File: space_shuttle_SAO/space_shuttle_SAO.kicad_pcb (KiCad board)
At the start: 2 copper layers, 80 x 49.8 mm, 4 parts, among them J1 SAO_1.69

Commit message: Working on the main village base badge
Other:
- net class Default removed

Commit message: updated per latest protoype discoveries
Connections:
- J1 pad 3: Net-(J1-Pad3) -> unconnected-(J1-Pad3)
- J1 pad 4: Net-(J1-Pad4) -> unconnected-(J1-Pad4)
- J1 pad 5: Net-(J1-Pad5) -> unconnected-(J1-Pad5)
- J1 pad 6: Net-(J1-Pad6) -> unconnected-(J1-Pad6)
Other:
- board text added: "aerospacevillage.org"
- board text added: "v03"
- board text removed: "v0.2"
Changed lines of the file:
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@@
   )
   (paper "A4")
+  (title_block
+    (title "Space Shuttle SAO")
+    (date "2022-05-22")
+    (rev "v03")
+    (company "Aerospace Village")
+    (comment 1 "Author: Dan Allen")
+  )
   (layers
     (0 "F.Cu" signal)
@@
   (net 2 "GND")
   (net 3 "Net-(J1-Pad1)")
-  (net 4 "Net-(J1-Pad3)")
-  (net 5 "Net-(J1-Pad4)")
-  (net 6 "Net-(J1-Pad5)")
-  (net 7 "Net-(J1-Pad6)")
+  (net 4 "unconnected-(J1-Pad3)")
+  (net 5 "unconnected-(J1-Pad4)")
+  (net 6 "unconnected-(J1-Pad5)")
+  (net 7 "unconnected-(J1-Pad6)")
   (footprint "space_shuttle_SAO:space_shuttle_proper" (layer "F.Cu")
     (at 140.51788 73.48728)
@@
   (footprint "space_shuttle_SAO:sao_1.69" (layer "F.Cu")
     (at 115.019626 99.883299 -20)
+    (property "Sheetfile" "space_shuttle_SAO.kicad_sch")
+    (property "Sheetname" "")
     (attr through_hole)
     (fp_text reference "J1" (at -0.04318 2.9337 160) (layer "F.SilkS") hide
@@
     )
     (pad "1" thru_hole rect locked (at -2.54 -1.27 340) (size 1.524 1.524) (drill 0.762) (layers *.Cu *.Mask)
-      (net 3 "Net-(J1-Pad1)"))
+      (net 3 "Net-(J1-Pad1)") (pinfunction "VCC") (pintype "passive"))
     (pad "2" thru_hole circle locked (at -2.54 1.27 340) (size 1.524 1.524) (drill 0.762) (layers *.Cu *.Mask)
-      (net 2 "GND"))
+      (net 2 "GND") (pinfunction "GND") (pintype "passive"))
     (pad "3" thru_hole circle locked (at 0 -1.27 340) (size 1.524 1.524) (drill 0.762) (layers *.Cu *.Mask)
-      (net 4 "Net-(J1-Pad3)"))
+      (net 4 "unconnected-(J1-Pad3)") (pinfunction "SDA") (pintype "passive+no_connect"))
     (pad "4" thru_hole circle locked (at 0 1.27 340) (size 1.524 1.524) (drill 0.762) (layers *.Cu *.Mask)
-      (net 5 "Net-(J1-Pad4)"))
+      (net 5 "unconnected-(J1-Pad4)") (pinfunction "SCL") (pintype "passive+no_connect"))
     (pad "5" thru_hole circle locked (at 2.54 -1.27 340) (size 1.524 1.524) (drill 0.762) (layers *.Cu *.Mask)
-      (net 6 "Net-(J1-Pad5)"))
+      (net 6 "unconnected-(J1-Pad5)") (pinfunction "GPIO_1") (pintype "passive+no_connect"))
     (pad "6" thru_hole circle locked (at 2.54 1.27 340) (size 1.524 1.524) (drill 0.762) (layers *.Cu *.Mask)
-      (net 7 "Net-(J1-Pad6)"))
+      (net 7 "unconnected-(J1-Pad6)") (pinfunction "GPIO_2") (pintype "passive+no_connect"))
   )
   (footprint "sunled:XZMYK45WT-9" (layer "B.Cu")
     (at 166.670202 106.777002 -45)
+    (property "Sheetfile" "space_shuttle_SAO.kicad_sch")
+    (property "Sheetname" "")
     (attr through_hole)
     (fp_text reference "D1" (at 5.10286 0.325119 45) (layer "B.SilkS")
@@
       (effects (font (size 1 1) (thickness 0.15)))
     )
-    (fp_circle (center 3.673303 1.655371) (end 3.873303 1.655371) (layer "B.SilkS") (width 0.4) (fill none))
+    (fp_circle (center -3.69824 -1.5621) (end -3.49824 -1.5621) (layer "B.SilkS") (width 0.4) (fill none))
     (fp_circle (center -0.01524 -0.14214) (end 0.78476 -0.14214) (layer "B.Mask") (width 1.6) (fill none))
     (pad "1" smd rect locked (at -2.6 0 315) (size 1.4 2.6) (layers "B.Cu" "B.Paste" "B.Mask")
-      (net 2 "GND"))
+      (net 2 "GND") (pinfunction "K") (pintype "passive"))
     (pad "2" smd rect locked (at 2.6 0 315) (size 1.4 2.6) (layers "B.Cu" "B.Paste" "B.Mask")
-      (net 1 "Net-(D1-Pad2)"))
+      (net 1 "Net-(D1-Pad2)") (pinfunction "A") (pintype "passive"))
   )
   (footprint "Resistors_SMD:R_1206_3216Metric" (layer "B.Cu")
@@
     (descr "Resistor SMD 1206 (3216 Metric), square (rectangular) end terminal, IPC_7351 nominal, (Body size source: IPC-SM-782 page 72, https://www.pcb-3d.com/wordpress/wp-content/uploads/ipc-sm-782a_amendment_1_and_2.pdf), generated with kicad-footprint-generator")
     (tags "resistor")
+    (property "Sheetfile" "space_shuttle_SAO.kicad_sch")
+    (property "Sheetname" "")
     (attr smd)
     (fp_text reference "R1" (at 0 1.82 -45) (layer "B.SilkS")
@@
     (fp_line (start 1.6 -0.8) (end -1.6 -0.8) (layer "B.Fab") (width 0.1))
     (pad "1" smd roundrect locked (at -1.4625 0 315) (size 1.125 1.75) (layers "B.Cu" "B.Paste" "B.Mask") (roundrect_rratio 0.2222204444)
-      (net 3 "Net-(J1-Pad1)"))
+      (net 3 "Net-(J1-Pad1)") (pintype "passive"))
     (pad "2" smd roundrect locked (at 1.4625 0 315) (size 1.125 1.75) (layers "B.Cu" "B.Paste" "B.Mask") (roundrect_rratio 0.2222204444)
-      (net 1 "Net-(D1-Pad2)"))
+      (net 1 "Net-(D1-Pad2)") (pintype "passive"))
     (model "${KISYS3DMOD}/Resistor_SMD.3dshapes/R_1206_3216Metric.wrl"
       (offset (xyz 0 0 0))
@@
     )
   )
-  (gr_text "v0.2" (at 108.51896 115.7224) (layer "B.Cu")
+  (gr_text "v03" (at 108.51896 115.7224) (layer "B.Cu")
     (effects (font (size 1.5 1.5) (thickness 0.3)) (justify mirror))
   )
@@
     (effects (font (size 1 1) (thickness 0.15)) (justify mirror))
   )
-  (gr_text "SAO V.1.69" (at 117.094 95.81896) (layer "B.SilkS")
+  (gr_text "aerospacevillage.org" (at 136.121177 96.432338 -20) (layer "B.SilkS")
+    (effects (font (size 3 3) (thickness 0.5)) (justify mirror))
+  )
+  (gr_text "SAO V.1.69" (at 116.934329 95.213789 -20) (layer "B.SilkS")
     (effects (font (size 1 1) (thickness 0.15)) (justify mirror))
   )
@@
   (zone (net 2) (net_name "GND") (layer "F.Cu") (hatch edge 0.508)
     (connect_pads (clearance 0.508))
-    (min_thickness 0.254)
+    (min_thickness 0.254) (filled_areas_thickness no)
     (fill yes (thermal_gap 0.508) (thermal_bridge_width 0.508))
     (polygon
@@
   (zone (net 2) (net_name "GND") (layer "B.Cu") (hatch edge 0.508)
     (connect_pads (clearance 0.508))
-    (min_thickness 0.254)
+    (min_thickness 0.254) (filled_areas_thickness no)
     (fill yes (thermal_gap 0.508) (thermal_bridge_width 0.508))
     (polygon

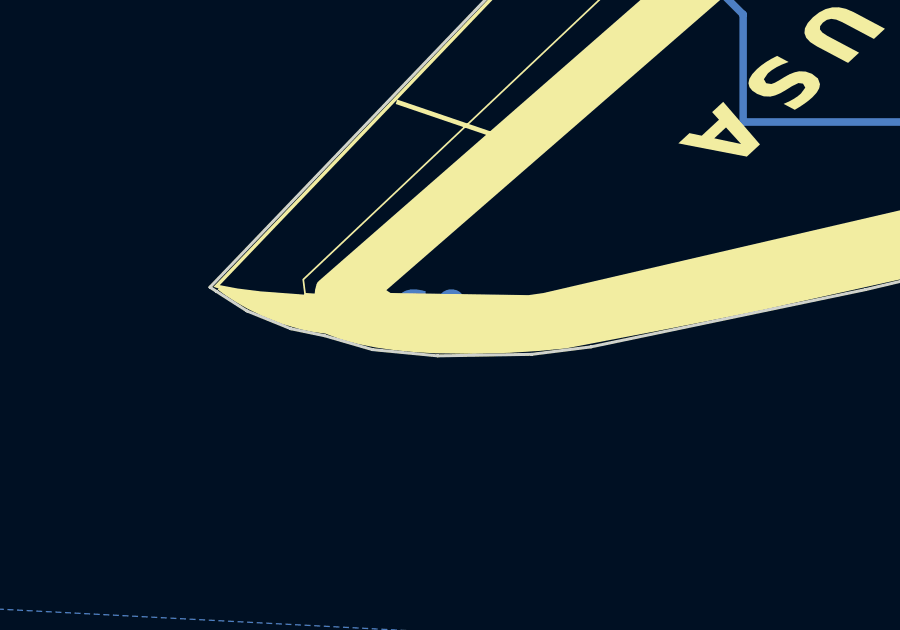
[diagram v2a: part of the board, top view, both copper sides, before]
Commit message: updated base badge, shuttle, and warning
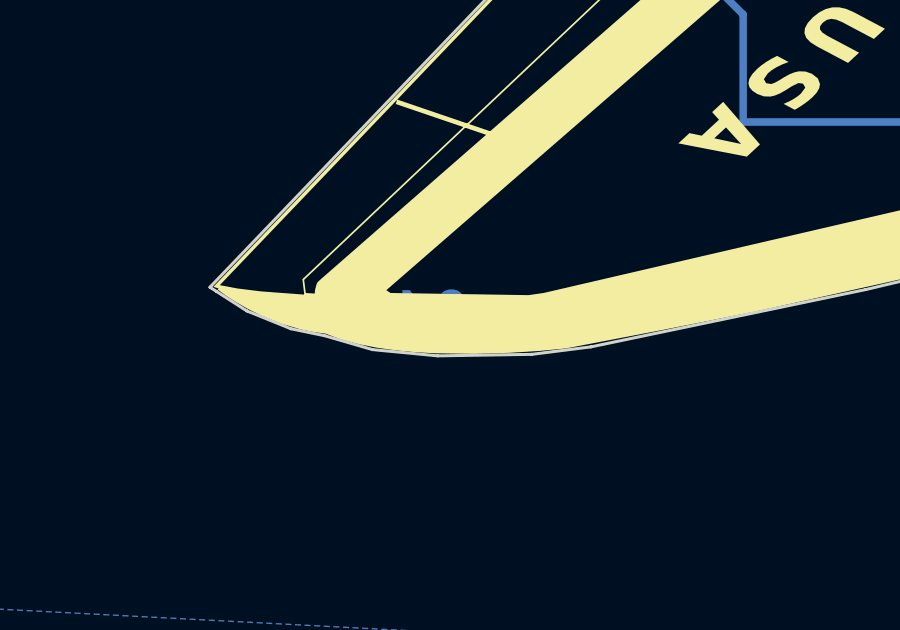
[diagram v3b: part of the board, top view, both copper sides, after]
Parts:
- added svg2mod: G***, aerospace_badge:aerospace_logo_new, B.Cu at (137.3, 104.2)
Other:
- board text added: "v04"
- board text removed: "v03"
